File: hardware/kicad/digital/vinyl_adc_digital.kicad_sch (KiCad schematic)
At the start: 13 parts, among them J1 CLK SEL, J2 TO PI GPIO, J4 2x8 BUS, U3 74HCT132, U4 74HC4040, U6 74HC157, U8 74HC4049, X1 6.144MHz

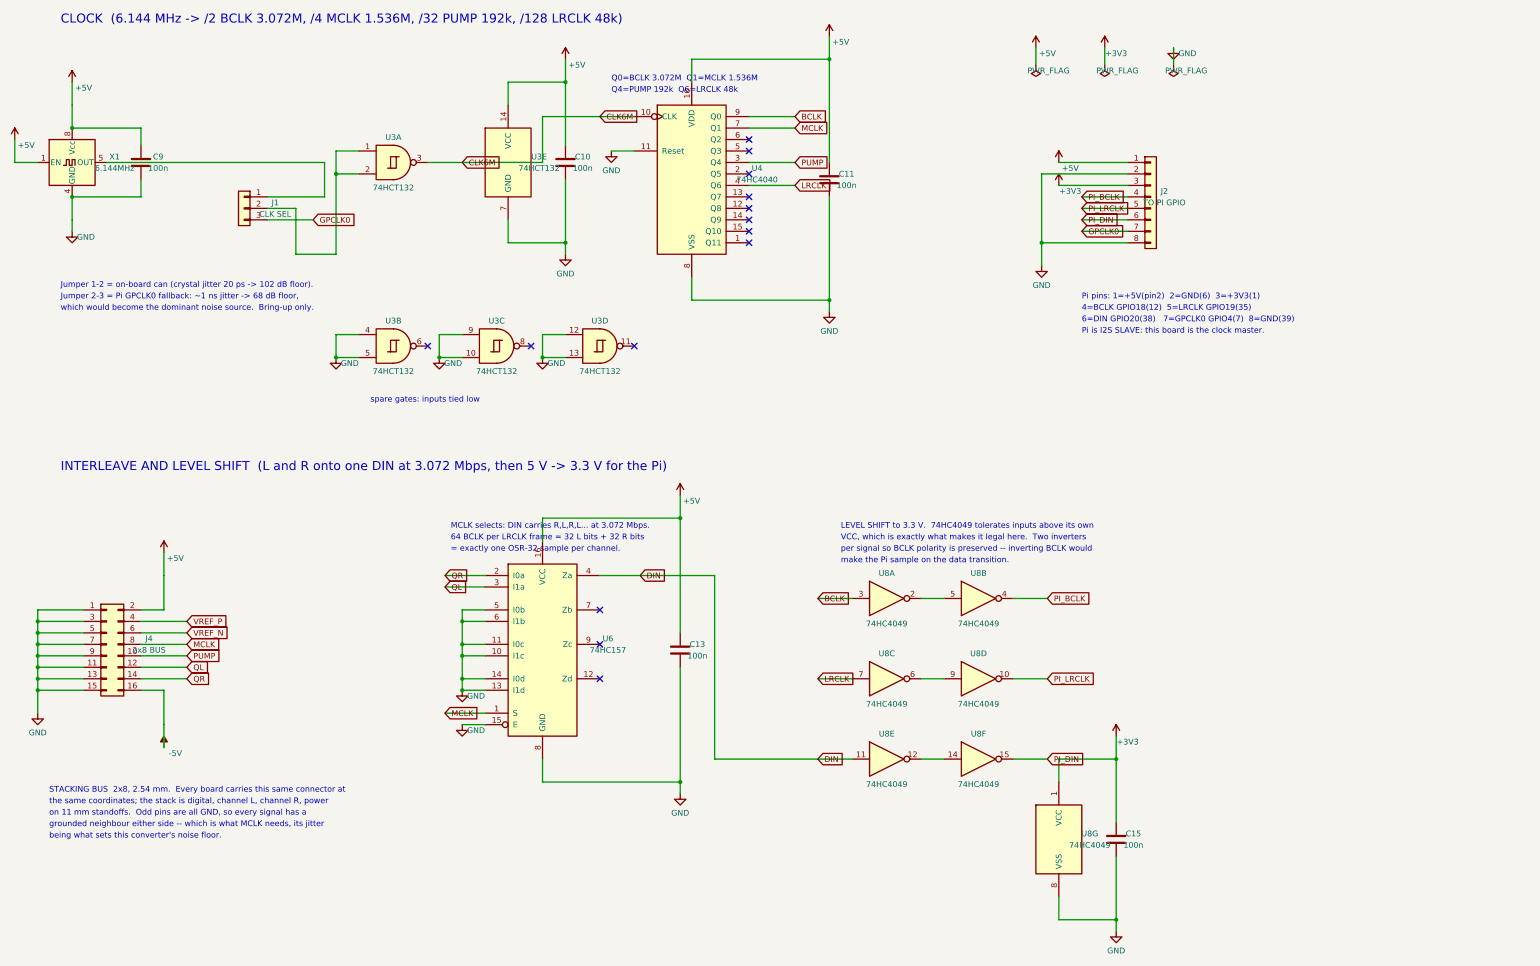
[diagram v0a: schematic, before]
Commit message: Replace the unobtainable oscillator can with a crystal Pierce
The 6.144 MHz can never turned up, but a bare 2-pin crystal did. The clock
is now a Pierce oscillator -- unbuffered 74HCU04, Rf 1M, Rs 2k2, 27p loads --
drawn by one shared blk_pierce so the digital board rev B, the plug-in
module and the sim_i_pierce bench cannot drift apart.

Rs is 2k2 and not the textbook 1k because the bench showed 1k lets the loop
oscillate at ~30 MHz through the crystal's 5 pF holder capacitance, and a
buffered 74HC04 re-lights that parasitic at any Rs; both findings are in
design-notes section 5 and asserted by the bench (suite 55/55).

The module (hardware/kicad/osc_module/) fills rev A's X1 socket: 40x44 mm
single-sided, routed clean, zero bridges, production files exported. The
digital rev B board carries the 4/4 placement with the bus and holes locked
at the stack coordinates, GND poured, routing still open at 13 links against
a floor of 3 -- same single-sided wall rev A hit, parked for now.

Tooling now runs on Linux too: portable paths in the layout/check/bom
scripts, and check_intent grew Pierce topology assertions.
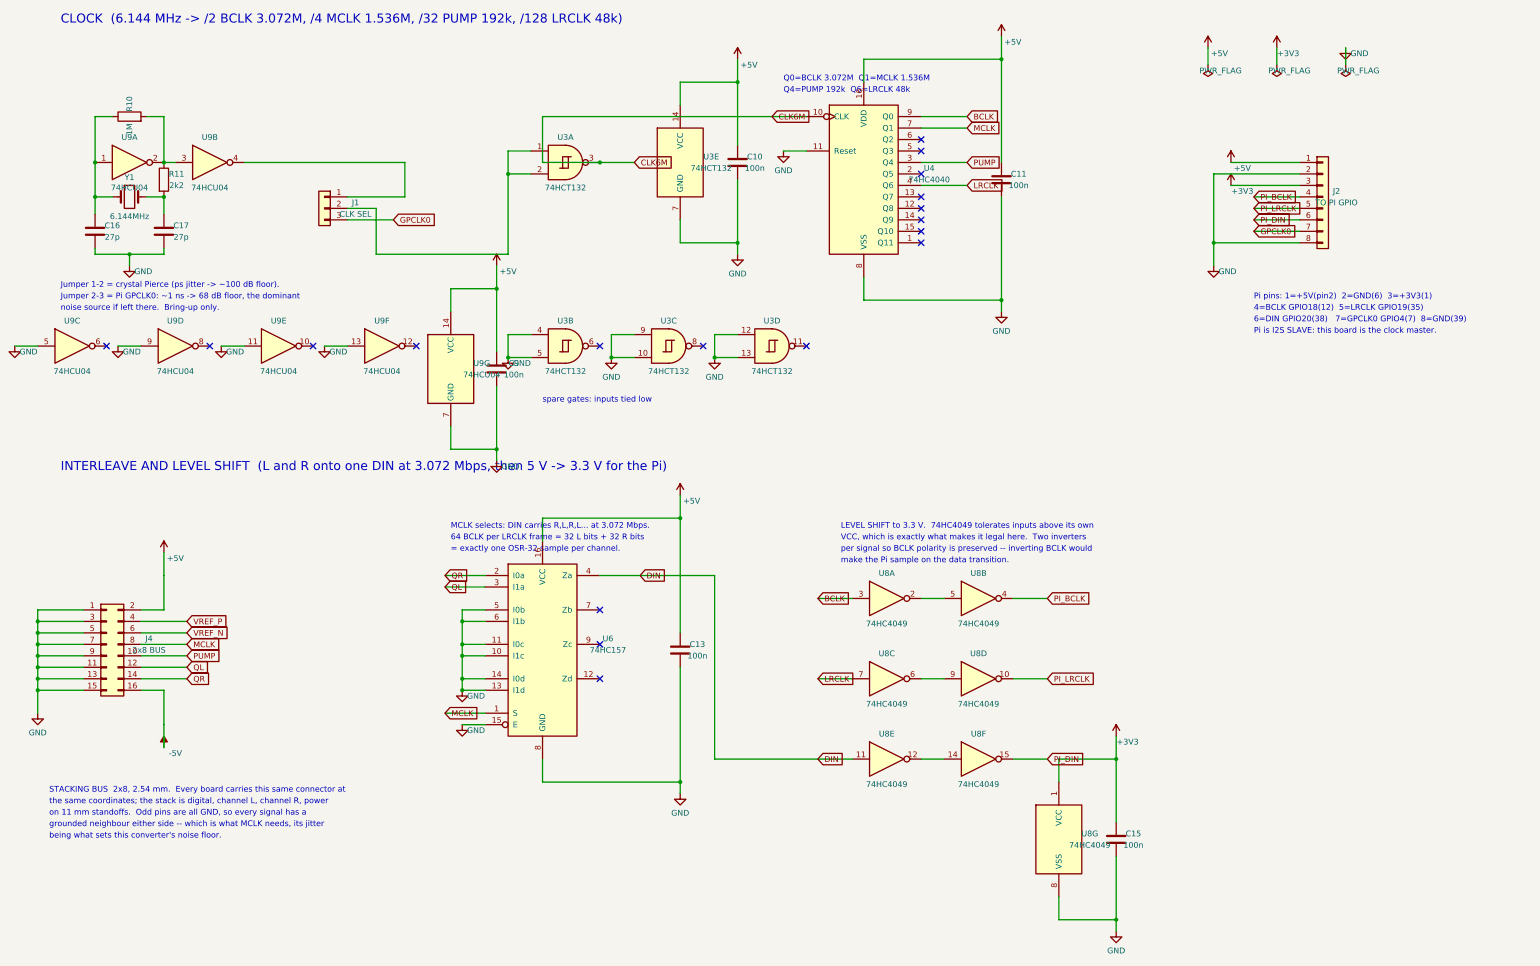
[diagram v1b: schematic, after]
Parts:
- removed X1: 6.144MHz, Package_DIP:DIP-8_W7.62mm_LongPads, symbol Oscillator:CXO_DIP8
- added C16, C17: 27p, Capacitor_THT:C_Disc_D5.0mm_W2.5mm_P5.00mm, symbol Device:C
- added R10: 1M, Resistor_THT:R_Axial_DIN0207_L6.3mm_D2.5mm_P7.62mm_Horizontal, symbol Device:R
- added R11: 2k2, Resistor_THT:R_Axial_DIN0207_L6.3mm_D2.5mm_P7.62mm_Horizontal, symbol Device:R
- added U9: 74HCU04, Package_DIP:DIP-14_W7.62mm_LongPads, symbol 74xx:74HC04
- added Y1: 6.144MHz, Crystal:Crystal_HC49-U_Vertical, symbol Device:Crystal
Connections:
- net +5V: now also U9.14 (VCC)
- net GND: now also C16.2, C17.2, U9.11, U9.13, U9.5, U9.7 (GND), U9.9
- net at J1.1 (Pin_1): now also U9.4
- new net: C16.1, R10.1, U9.1, Y1.1
- new net: C17.1, R11.2, Y1.2
- new net: R10.2, R11.1, U9.2, U9.3
- no-connect marks 14 -> 18
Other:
- note added: "Jumper 1-2 = crystal Pierce (ps jitter -> ~100 dB floor)."
- note added: "Jumper 2-3 = Pi GPCLK0: ~1 ns -> 68 dB floor, the dominant"
- note added: "noise source if left there. Bring-up only."
- note removed: "Jumper 1-2 = on-board can (crystal jitter 20 ps -> 102 dB floor)."
- note removed: "Jumper 2-3 = Pi GPCLK0 fallback: ~1 ns jitter -> 68 dB floor,"
- note removed: "which would become the dominant noise source. Bring-up only."
